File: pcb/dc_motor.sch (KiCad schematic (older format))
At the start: 64 parts, among them J1 Conn_01x02, J2 Conn_01x02, J3 Conn_01x04, J4 Conn_01x07, J5 Conn_01x02, Q1 IPD50P04P4L11, Q2 BTN8962, Q3 BTN8962, U1 L7805, U2 INA226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

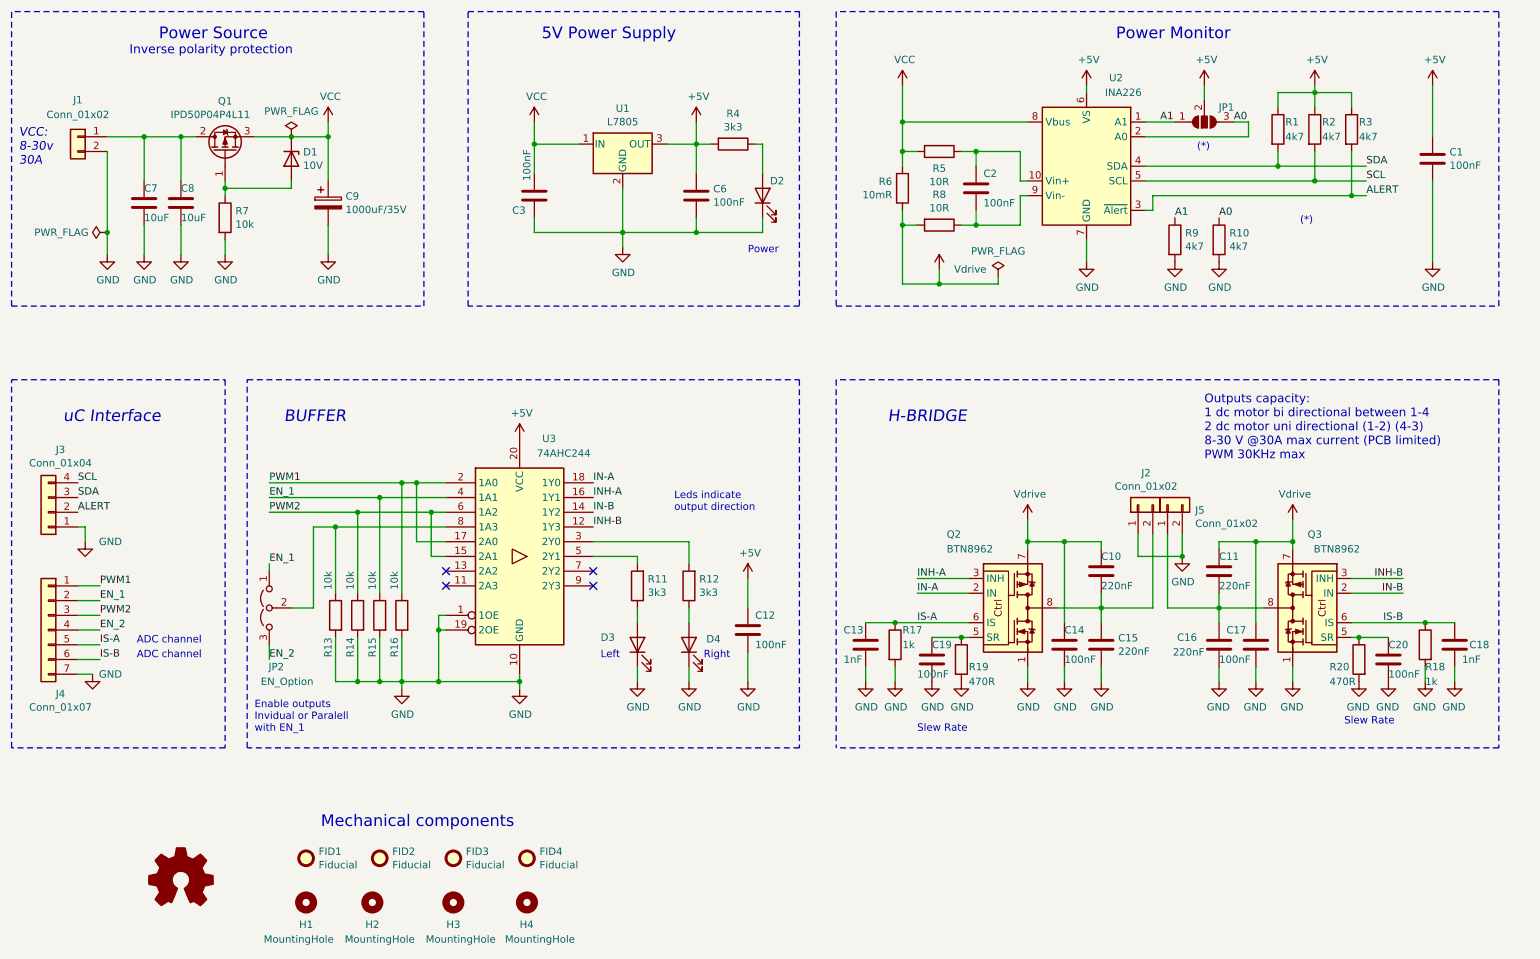
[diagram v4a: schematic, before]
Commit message: Rev 1.1
Change power connectors and limited current to 20A
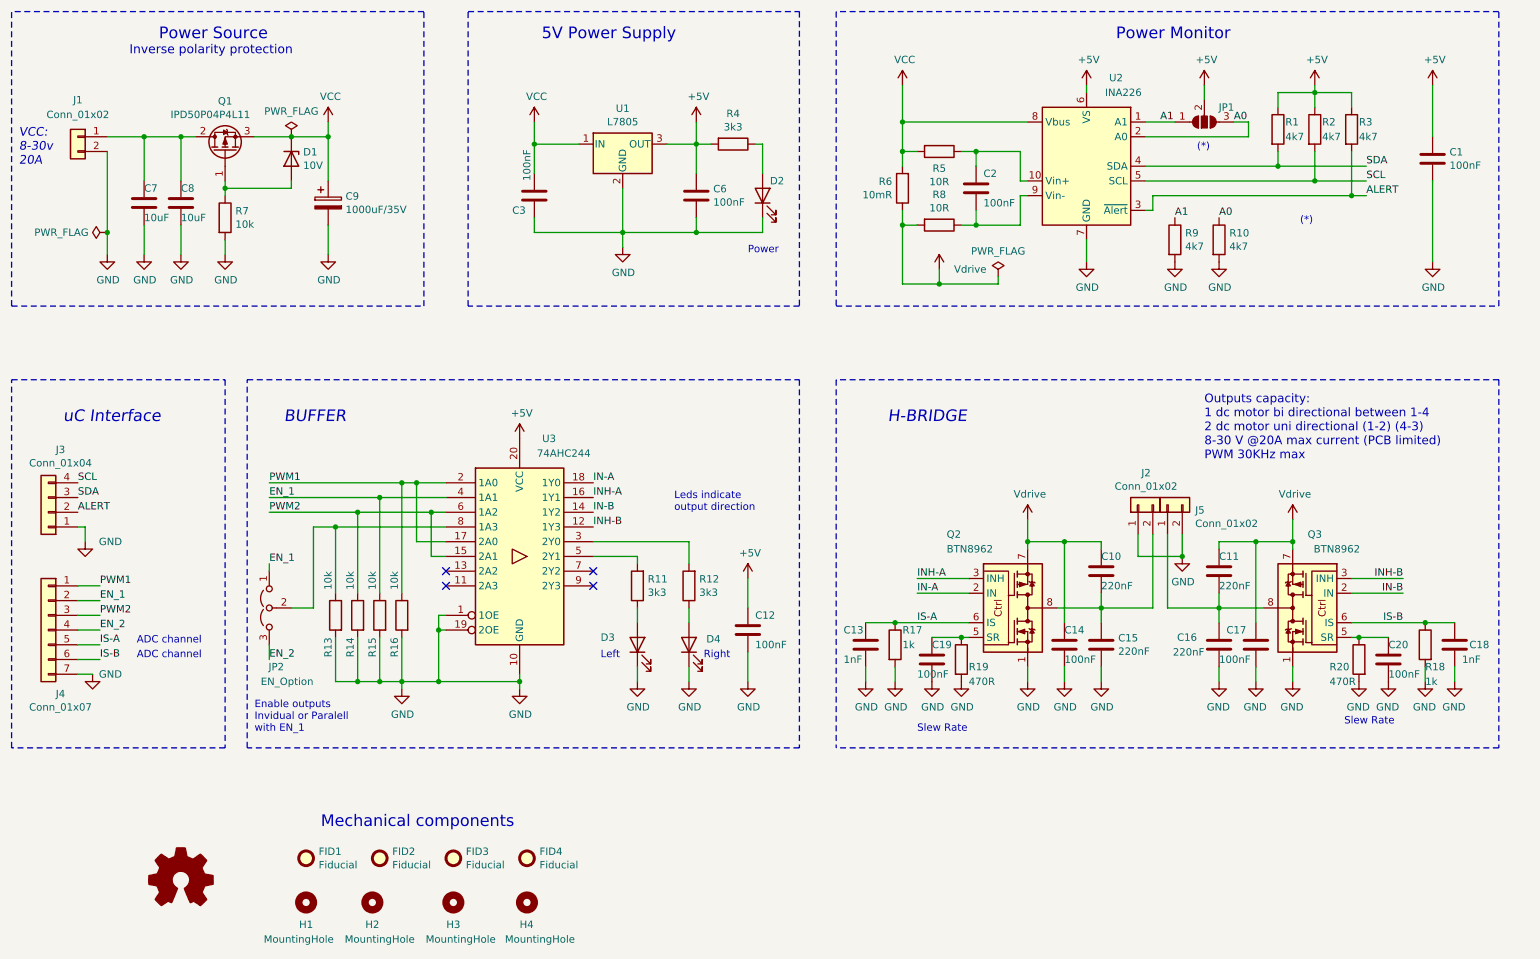
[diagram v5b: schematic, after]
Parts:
- J1, J2, J5: digikey# 281-8216-ND -> 732-2052-ND; manf# 1837980000 -> 691311500002
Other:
- note added: "Outputs capacity:\n1 dc motor bi directional between 1-4\n2 dc motor uni directional (1-2) (4-3)\n8-30 V @20A max current (PCB limited)\nPWM 30KHz max"
- note added: "VCC:\n8-30v\n20A"
- note removed: "Outputs capacity:\n1 dc motor bi directional between 1-4\n2 dc motor uni directional (1-2) (4-3)\n8-30 V @30A max current (PCB limited)\nPWM 30KHz max"
- note removed: "VCC:\n8-30v\n30A"
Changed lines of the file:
@@
 Sheet 1 1
 Title "DC MOTOR CONTROL"
-Date "2020-11-04"
-Rev "1.0"
+Date "2020-11-15"
+Rev "1.1"
 Comp "NOVOTEC ARGENTINA SRL"
 Comment1 "Author: Ing. Luciano Vittori"
@@
 	11000 6000 6500 6000
 Text Notes 9000 4050 0    59   ~ 0
-Outputs capacity:\n1 dc motor bi directional between 1-4\n2 dc motor uni directional (1-2) (4-3)\n8-30 V @30A max current (PCB limited)\nPWM 30KHz max
+Outputs capacity:\n1 dc motor bi directional between 1-4\n2 dc motor uni directional (1-2) (4-3)\n8-30 V @20A max current (PCB limited)\nPWM 30KHz max
 $Comp
 L Device:R R16
@@
 F 1 "BTN8962" H 9500 5450 50  0000 C CNN
 F 2 "Package_TO_SOT_SMD:TO-263-7_TabPin8" H 9500 5500 50  0001 C CNN
-F 3 "https://www.infineon.com/dgdl/Infineon-BTN8982TA-DS-v01_00-EN.pdf?fileId=db3a30433fa9412f013fbe32289b7c17" H 9650 5060 50  0001 C CNN
+F 3 "https://www.infineon.com/dgdl/BTN8962TA-Data-Sheet-rev10-Infineon.pdf?folderId=db3a30431ff98815012060aedcd46179&fileId=db3a30433fa9412f013fbe2d247a7bf5&ack=t" H 9650 5060 50  0001 C CNN
 F 4 "BTN8962TAAUMA1INCT-ND" H 9700 5050 50  0001 C CNN "manf#"
 F 5 "BTN8962TAAUMA1" H 9700 5050 50  0001 C CNN "digikey#"
@@
 $EndBitmap
 Text Notes 950  2050 0    59   Italic 0
-VCC:\n8-30v\n30A
+VCC:\n8-30v\n20A
 Wire Wire Line
 	6950 1750 6950 1950
@@
 F 1 "Conn_01x02" H 1350 2000 50  0000 C CNN
 F 2 "Connector_Phoenix_MC_HighVoltage:PhoenixContact_MCV_1,5_2-G-5.08_1x02_P5.08mm_Vertical" H 1350 1850 50  0001 C CNN
-F 3 "~" H 1350 1850 50  0001 C CNN
-F 4 "1837980000" H 1350 1850 50  0001 C CNN "manf#"
-F 5 "281-8216-ND" H 1350 1850 50  0001 C CNN "digikey#"
+F 3 "https://www.we-online.de/katalog/datasheet/6913115000xx.pdf" H 1350 1850 50  0001 C CNN
+F 4 "691311500002" H 1350 1850 50  0001 C CNN "manf#"
+F 5 "732-2052-ND" H 1350 1850 50  0001 C CNN "digikey#"
 	1    1350 1850
 	-1   0    0    -1
@@
 F 1 "BTN8962" H 7250 5450 50  0000 L CNN
 F 2 "Package_TO_SOT_SMD:TO-263-7_TabPin8" H 7500 5500 50  0001 C CNN
-F 3 "https://www.infineon.com/dgdl/Infineon-BTN8982TA-DS-v01_00-EN.pdf?fileId=db3a30433fa9412f013fbe32289b7c17" H 7650 5060 50  0001 C CNN
+F 3 "https://www.infineon.com/dgdl/BTN8962TA-Data-Sheet-rev10-Infineon.pdf?folderId=db3a30431ff98815012060aedcd46179&fileId=db3a30433fa9412f013fbe2d247a7bf5&ack=t" H 7650 5060 50  0001 C CNN
 F 4 "BTN8962TAAUMA1INCT-ND" H 7700 5050 50  0001 C CNN "manf#"
 F 5 "BTN8962TAAUMA1" H 7700 5050 50  0001 C CNN "digikey#"
@@
 F 1 "Conn_01x02" V 8676 4296 50  0000 C CNN
 F 2 "Connector_Phoenix_MC_HighVoltage:PhoenixContact_MCV_1,5_2-G-5.08_1x02_P5.08mm_Vertical" H 8550 4350 50  0001 C CNN
-F 3 "~" H 8550 4350 50  0001 C CNN
-F 4 "1837980000" H 8550 4350 50  0001 C CNN "manf#"
-F 5 "281-8216-ND" H 8550 4350 50  0001 C CNN "digikey#"
+F 3 "https://www.we-online.de/katalog/datasheet/6913115000xx.pdf" H 8550 4350 50  0001 C CNN
+F 4 "691311500002" H 8550 4350 50  0001 C CNN "manf#"
+F 5 "732-2052-ND" H 8550 4350 50  0001 C CNN "digikey#"
 	1    8550 4350
 	0    -1   -1   0
@@
 F 1 "Conn_01x02" V 8623 4162 50  0000 R CNN
 F 2 "Connector_Phoenix_MC_HighVoltage:PhoenixContact_MCV_1,5_2-G-5.08_1x02_P5.08mm_Vertical" H 8750 4350 50  0001 C CNN
-F 3 "~" H 8750 4350 50  0001 C CNN
-F 4 "1837980000" H 8750 4350 50  0001 C CNN "manf#"
-F 5 "281-8216-ND" H 8750 4350 50  0001 C CNN "digikey#"
+F 3 "https://www.we-online.de/katalog/datasheet/6913115000xx.pdf" H 8750 4350 50  0001 C CNN
+F 4 "691311500002" H 8750 4350 50  0001 C CNN "manf#"
+F 5 "732-2052-ND" H 8750 4350 50  0001 C CNN "digikey#"
 	1    8750 4350
 	0    -1   -1   0
